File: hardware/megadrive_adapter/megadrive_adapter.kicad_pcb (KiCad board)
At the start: 2 copper layers, 96.6 x 25.5 mm, 3 parts, among them J1 CART SLOT TOP ROW, J2 CART SLOT BOTTOM ROW, U1 MD_Slot

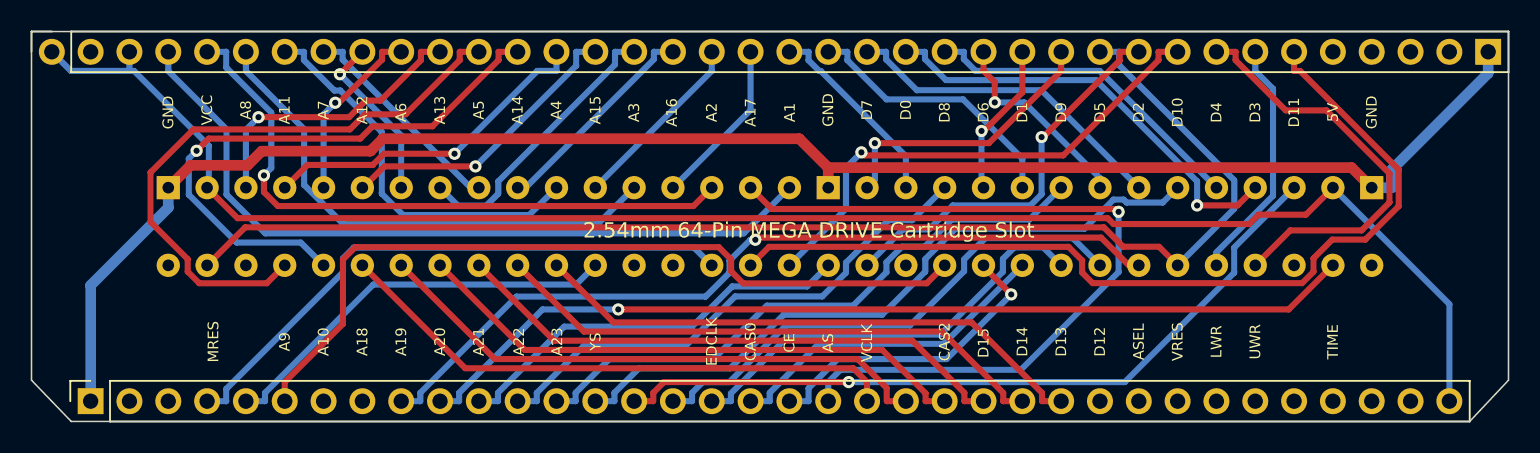
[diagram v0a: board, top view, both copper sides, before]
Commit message: Fix MD and NES adapter PCBs and add Famicom adapter
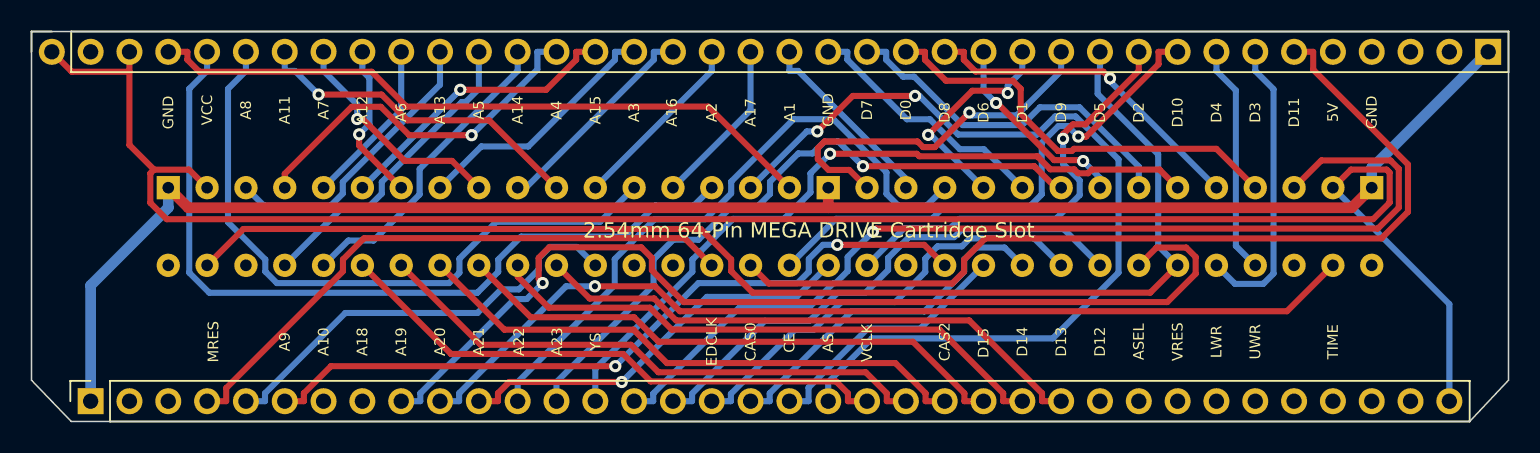
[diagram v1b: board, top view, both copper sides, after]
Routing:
- net A8: track 39.7 -> 20.4 mm
- net A9: track 37.8 -> 20.2 mm, vias 1 -> 0
- net D25: track 50.3 -> 66.5 mm
- net VCC: track 109.6 -> 125.6 mm
- net D7: track 27.3 -> 15.0 mm
- net D4: track 54.2 -> 66.1 mm
- net A1: track 42.0 -> 53.0 mm, vias 1 -> 0
- net A2: track 33.9 -> 43.4 mm
- net D49: track 51.9 -> 59.9 mm, vias 1 -> 2
- net D22: track 34.4 -> 41.4 mm
- net D30: track 18.5 -> 24.4 mm
- net A0: track 50.0 -> 44.6 mm
- net D31: track 10.1 -> 14.6 mm, vias 1 -> 2
- net D23: track 39.5 -> 43.5 mm, vias 0 -> 1
- net D3: track 52.5 -> 48.8 mm, vias 0 -> 2
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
